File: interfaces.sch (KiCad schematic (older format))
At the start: 16 parts, among them U10 TDA19988BHN_C1,557

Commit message: Update naming convention
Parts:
- C37, C39, C41, C43: footprint arv-som-footprints:0402-cap -> arvsom-footprints:0402-cap; symbol arv-som:C_2u2_0402 -> arvsom:C_2u2_0402
- C38, C40, C42, C44: footprint arv-som-footprints:0201-res -> arvsom-footprints:0201-res; symbol arv-som:C_100n_0201 -> arvsom:C_100n_0201
- D3: footprint arv-som-footprints:SOD-323F -> arvsom-footprints:SOD-323F; symbol arv-som:1N4148WS -> arvsom:1N4148WS
- FB1, FB7: footprint arv-som-footprints:0402-res -> arvsom-footprints:0402-res; symbol arv-som:BLM15PD121SN1D -> arvsom:BLM15PD121SN1D
- R25: footprint arv-som-footprints:0402-res -> arvsom-footprints:0402-res; symbol arv-som:R_10k_0402 -> arvsom:R_10k_0402
- R26, R27: footprint arv-som-footprints:0402-res -> arvsom-footprints:0402-res; symbol arv-som:R_1k_0402 -> arvsom:R_1k_0402
- R28: footprint arv-som-footprints:0402-res -> arvsom-footprints:0402-res; symbol arv-som:R_27k_0402 -> arvsom:R_27k_0402
- U10: footprint arv-som-footprints:QFN50P900X900X100-65N -> arvsom-footprints:QFN50P900X900X100-65N; symbol arv-som:TDA19988BHN_C1,557 -> arvsom:TDA19988BHN_C1,557
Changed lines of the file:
@@
 $EndDescr
 $Comp
-L arv-som:TDA19988BHN_C1,557 U10
+L arvsom:TDA19988BHN_C1,557 U10
 U 1 1 607A5735
 P 7075 5525
 F 0 "U10" H 7075 8192 50  0000 C CNN
 F 1 "TDA19988BHN_C1,557" H 7075 8101 50  0000 C CNN
-F 2 "arv-som-footprints:QFN50P900X900X100-65N" H 7075 5525 50  0001 L BNN
+F 2 "arvsom-footprints:QFN50P900X900X100-65N" H 7075 5525 50  0001 L BNN
 F 3 "" H 7075 5525 50  0001 L BNN
 F 4 "NXP Semiconductors" H 7075 5525 50  0001 L BNN "MANUFACTURER"
@@
 Connection ~ 5975 3725
 $Comp
-L arv-som:GND #PWR0137
+L arvsom:GND #PWR0137
 U 1 1 607C5297
 P 5975 8125
@@
 Connection ~ 8375 3425
 $Comp
-L arv-som:C_2u2_0402 C37
+L arvsom:C_2u2_0402 C37
 U 1 1 607E47D0
 P 9125 3000
 F 0 "C37" H 9240 3045 60  0000 L CNN
 F 1 "C_2u2_0402" H 9125 2850 60  0001 C CNN
-F 2 "arv-som-footprints:0402-cap" H 9325 3200 60  0001 L CNN
+F 2 "arvsom-footprints:0402-cap" H 9325 3200 60  0001 L CNN
 F 3 "" H 9125 3000 50  0001 C CNN
 F 4 "TDK" H 9325 3400 60  0001 L CNN "Manufacturer"
@@
 $EndComp
 $Comp
-L arv-som:C_2u2_0402 C39
+L arvsom:C_2u2_0402 C39
 U 1 1 607E4C5F
 P 9900 3000
 F 0 "C39" H 10015 3045 60  0000 L CNN
 F 1 "C_2u2_0402" H 9900 2850 60  0001 C CNN
-F 2 "arv-som-footprints:0402-cap" H 10100 3200 60  0001 L CNN
+F 2 "arvsom-footprints:0402-cap" H 10100 3200 60  0001 L CNN
 F 3 "" H 9900 3000 50  0001 C CNN
 F 4 "TDK" H 10100 3400 60  0001 L CNN "Manufacturer"
@@
 HDMI_1V8
 $Comp
-L arv-som:GND #PWR0138
+L arvsom:GND #PWR0138
 U 1 1 607E87FB
 P 9125 3150
@@
 HDMI_1V8
 $Comp
-L arv-som:GND #PWR0139
+L arvsom:GND #PWR0139
 U 1 1 607EFCC2
 P 9900 3150
@@
 $EndComp
 $Comp
-L arv-som:C_2u2_0402 C41
+L arvsom:C_2u2_0402 C41
 U 1 1 607F1ECB
 P 10625 3000
 F 0 "C41" H 10740 3045 60  0000 L CNN
 F 1 "C_2u2_0402" H 10625 2850 60  0001 C CNN
-F 2 "arv-som-footprints:0402-cap" H 10825 3200 60  0001 L CNN
+F 2 "arvsom-footprints:0402-cap" H 10825 3200 60  0001 L CNN
 F 3 "" H 10625 3000 50  0001 C CNN
 F 4 "TDK" H 10825 3400 60  0001 L CNN "Manufacturer"
@@
 HDMI_1V8
 $Comp
-L arv-som:GND #PWR0140
+L arvsom:GND #PWR0140
 U 1 1 607F1ED2
 P 10625 3150
@@
 $EndComp
 $Comp
-L arv-som:C_2u2_0402 C43
+L arvsom:C_2u2_0402 C43
 U 1 1 607F4B71
 P 11375 3000
 F 0 "C43" H 11490 3045 60  0000 L CNN
 F 1 "C_2u2_0402" H 11375 2850 60  0001 C CNN
-F 2 "arv-som-footprints:0402-cap" H 11575 3200 60  0001 L CNN
+F 2 "arvsom-footprints:0402-cap" H 11575 3200 60  0001 L CNN
 F 3 "" H 11375 3000 50  0001 C CNN
 F 4 "TDK" H 11575 3400 60  0001 L CNN "Manufacturer"
@@
 HDMI_1V8
 $Comp
-L arv-som:GND #PWR0141
+L arvsom:GND #PWR0141
 U 1 1 607F4B78
 P 11375 3150
@@
 $EndComp
 $Comp
-L arv-som:C_100n_0201 C38
+L arvsom:C_100n_0201 C38
 U 1 1 607F7307
 P 9500 3000
 F 0 "C38" H 9615 3045 60  0000 L CNN
 F 1 "C_100n_0201" H 9500 2850 60  0001 C CNN
-F 2 "arv-som-footprints:0201-res" H 9700 3200 60  0001 L CNN
+F 2 "arvsom-footprints:0201-res" H 9700 3200 60  0001 L CNN
 F 3 "" H 9500 3000 50  0001 C CNN
 F 4 "YAGEO" H 9700 3400 60  0001 L CNN "Manufacturer"
@@
 HDMI_1V8
 $Comp
-L arv-som:GND #PWR0142
+L arvsom:GND #PWR0142
 U 1 1 607F77A7
 P 9500 3150
@@
 $EndComp
 $Comp
-L arv-som:C_100n_0201 C40
+L arvsom:C_100n_0201 C40
 U 1 1 607F8E18
 P 10275 3000
 F 0 "C40" H 10390 3045 60  0000 L CNN
 F 1 "C_100n_0201" H 10275 2850 60  0001 C CNN
-F 2 "arv-som-footprints:0201-res" H 10475 3200 60  0001 L CNN
+F 2 "arvsom-footprints:0201-res" H 10475 3200 60  0001 L CNN
 F 3 "" H 10275 3000 50  0001 C CNN
 F 4 "YAGEO" H 10475 3400 60  0001 L CNN "Manufacturer"
@@
 HDMI_1V8
 $Comp
-L arv-som:GND #PWR0143
+L arvsom:GND #PWR0143
 U 1 1 607F8E1F
 P 10275 3150
@@
 $EndComp
 $Comp
-L arv-som:C_100n_0201 C42
+L arvsom:C_100n_0201 C42
 U 1 1 607FB340
 P 11000 3000
 F 0 "C42" H 11115 3045 60  0000 L CNN
 F 1 "C_100n_0201" H 11000 2850 60  0001 C CNN
-F 2 "arv-som-footprints:0201-res" H 11200 3200 60  0001 L CNN
+F 2 "arvsom-footprints:0201-res" H 11200 3200 60  0001 L CNN
 F 3 "" H 11000 3000 50  0001 C CNN
 F 4 "YAGEO" H 11200 3400 60  0001 L CNN "Manufacturer"
@@
 HDMI_1V8
 $Comp
-L arv-som:GND #PWR0144
+L arvsom:GND #PWR0144
 U 1 1 607FB347
 P 11000 3150
@@
 $EndComp
 $Comp
-L arv-som:C_100n_0201 C44
+L arvsom:C_100n_0201 C44
 U 1 1 607FD800
 P 11750 3000
 F 0 "C44" H 11865 3045 60  0000 L CNN
 F 1 "C_100n_0201" H 11750 2850 60  0001 C CNN
-F 2 "arv-som-footprints:0201-res" H 11950 3200 60  0001 L CNN
+F 2 "arvsom-footprints:0201-res" H 11950 3200 60  0001 L CNN
 F 3 "" H 11750 3000 50  0001 C CNN
 F 4 "YAGEO" H 11950 3400 60  0001 L CNN "Manufacturer"
@@
 HDMI_1V8
 $Comp
-L arv-som:GND #PWR0145
+L arvsom:GND #PWR0145
 U 1 1 607FD807
 P 11750 3150
@@
 TODO: 2u2 with 0201 package
 $Comp
-L arv-som:BLM15PD121SN1D FB1
+L arvsom:BLM15PD121SN1D FB1
 U 1 1 6086D39A
 P 11325 2175
 F 0 "FB1" H 11325 2462 60  0000 C CNN
 F 1 "BLM15PD121SN1D" H 11325 2356 60  0000 C CNN
-F 2 "arv-som-footprints:0402-res" H 11525 2375 60  0001 L CNN
+F 2 "arvsom-footprints:0402-res" H 11525 2375 60  0001 L CNN
 F 3 "" H 11525 2475 60  0001 L CNN
 F 4 "BLM15PD121SN1D" H 11525 2675 60  0001 L CNN "MPN"
@@
 	8550 3725 8650 3725
 $Comp
-L arv-som:R_10k_0402 R25
+L arvsom:R_10k_0402 R25
 U 1 1 608924F4
 P 8800 3725
 F 0 "R25" H 8800 3938 60  0000 C CNN
 F 1 "R_10k_0402" H 8800 3575 60  0001 C CNN
-F 2 "arv-som-footprints:0402-res" H 9000 3925 60  0001 L CNN
+F 2 "arvsom-footprints:0402-res" H 9000 3925 60  0001 L CNN
 F 3 "" H 8800 3725 50  0001 C CNN
 F 4 "VISHAY" H 9000 4125 60  0001 L CNN "Manufacturer"
@@
 $EndComp
 $Comp
-L arv-som:GND #PWR0146
+L arvsom:GND #PWR0146
 U 1 1 60893600
 P 9050 3725
@@
 HDMI_DSDA
 $Comp
-L arv-som:R_1k_0402 R26
+L arvsom:R_1k_0402 R26
 U 1 1 608F44D4
 P 9025 6125
 F 0 "R26" H 8950 6225 60  0000 L CNN
 F 1 "R_1k_0402" H 9025 5975 60  0001 C CNN
-F 2 "arv-som-footprints:0402-res" H 9225 6325 60  0001 L CNN
+F 2 "arvsom-footprints:0402-res" H 9225 6325 60  0001 L CNN
 F 3 "" H 9025 6125 50  0001 C CNN
 F 4 "BOURNS" H 9225 6525 60  0001 L CNN "Manufacturer"
@@
 $EndComp
 $Comp
-L arv-som:R_1k_0402 R27
+L arvsom:R_1k_0402 R27
 U 1 1 608F47DE
 P 9275 6125
 F 0 "R27" H 9200 6225 60  0000 L CNN
 F 1 "R_1k_0402" H 9275 5975 60  0001 C CNN
-F 2 "arv-som-footprints:0402-res" H 9475 6325 60  0001 L CNN
+F 2 "arvsom-footprints:0402-res" H 9475 6325 60  0001 L CNN
 F 3 "" H 9275 6125 50  0001 C CNN
 F 4 "BOURNS" H 9475 6525 60  0001 L CNN "Manufacturer"
@@
 HDMI_HPD
 $Comp
-L arv-som:1N4148WS D3
+L arvsom:1N4148WS D3
 U 1 1 60934FA2
 P 9225 6950
 F 0 "D3" H 9025 6900 60  0000 C CNN
 F 1 "1N4148WS" H 9575 6900 60  0000 C CNN
-F 2 "arv-som-footprints:SOD-323F" H 9425 7150 60  0001 L CNN
+F 2 "arvsom-footprints:SOD-323F" H 9425 7150 60  0001 L CNN
 F 3 "https://www.onsemi.com/pub/Collateral/1N914BWS-D.pdf" H 9425 7250 60  0001 L CNN
 F 4 "1N4148WS" H 9425 7450 60  0001 L CNN "MPN"
@@
 	8950 7125 9425 7125
 $Comp
-L arv-som:R_27k_0402 R28
+L arvsom:R_27k_0402 R28
 U 1 1 6093E329
 P 9700 6950
 F 0 "R28" H 9700 7050 60  0000 C CNN
 F 1 "R_27k_0402" H 9700 6800 60  0001 C CNN
-F 2 "arv-som-footprints:0402-res" H 9900 7150 60  0001 L CNN
+F 2 "arvsom-footprints:0402-res" H 9900 7150 60  0001 L CNN
 F 3 "" H 9700 6950 50  0001 C CNN
 F 4 "PANASONIC_ELECTRONIC_COMPONENTS" H 9900 7350 60  0001 L CNN "Manufacturer"
@@
 	8225 7825 8225 7925
 $Comp
-L arv-som:GND #PWR0147
+L arvsom:GND #PWR0147
 U 1 1 6095A132
 P 8225 8125
@@
 $EndBitmap
 $Comp
-L arv-som:BLM15PD121SN1D FB7
+L arvsom:BLM15PD121SN1D FB7
 U 1 1 60D6E8D3
 P 9025 5700
 F 0 "FB7" H 9025 5987 60  0000 C CNN
 F 1 "BLM15PD121SN1D" H 9025 5881 60  0000 C CNN
-F 2 "arv-som-footprints:0402-res" H 9225 5900 60  0001 L CNN
+F 2 "arvsom-footprints:0402-res" H 9225 5900 60  0001 L CNN
 F 3 "" H 9225 6000 60  0001 L CNN
 F 4 "BLM15PD121SN1D" H 9225 6200 60  0001 L CNN "MPN"

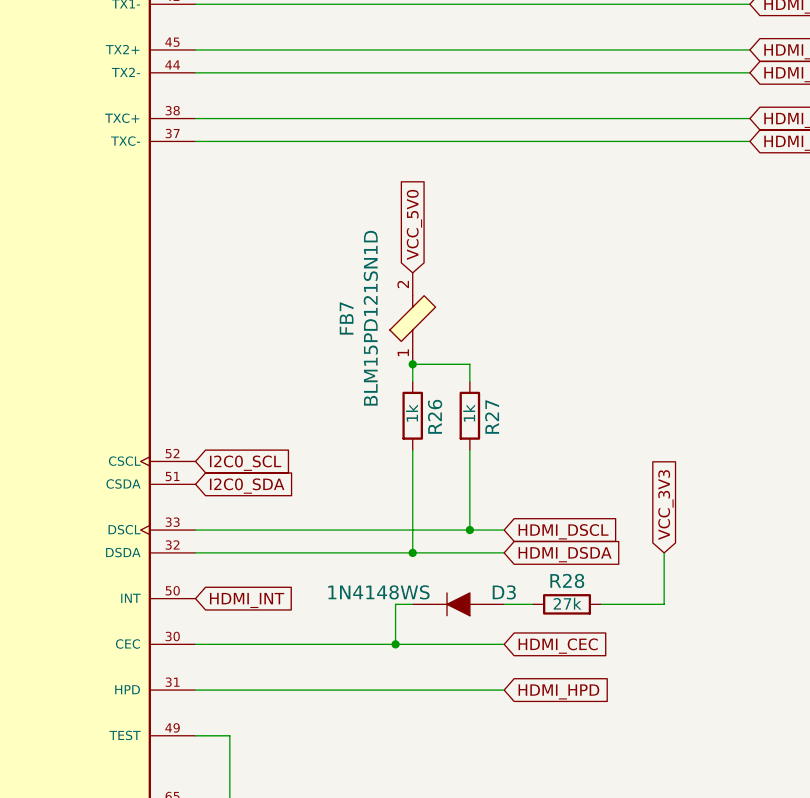
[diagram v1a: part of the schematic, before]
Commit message: Updated ethernet and interfaces.sch
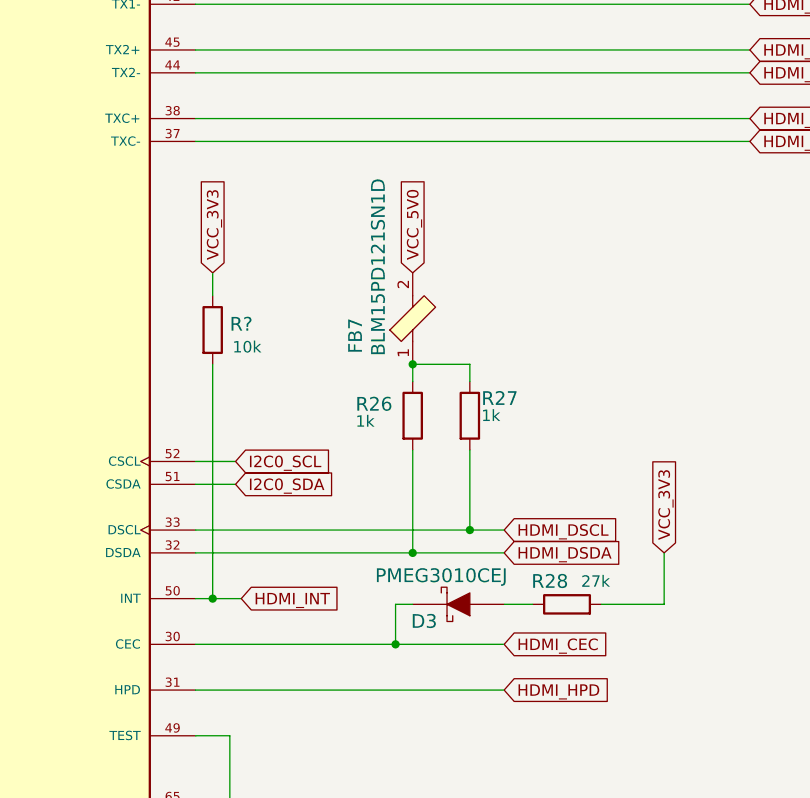
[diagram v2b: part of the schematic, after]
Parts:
- removed D3: 1N4148WS, arvsom-footprints:SOD-323F, symbol arvsom:1N4148WS
- added D3: PMEG3010CEJ, arvsom-footprints:SOD-323F, symbol arvsom:PMEG3010CEJ
- added R?: R_10k_0402, arvsom-footprints:0402-res, symbol arvsom:R_10k_0402
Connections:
- net HDMI_CEC: now also D3.K
- net HDMI_INT: now also R?.2
- net VCC_3V3: now also R?.1
- net at R28.1: now also D3.A
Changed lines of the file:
@@
 U 1 1 608F44D4
 P 9025 6125
-F 0 "R26" H 8950 6225 60  0000 L CNN
+F 0 "R26" V 8975 5875 60  0000 L CNN
 F 1 "R_1k_0402" H 9025 5975 60  0001 C CNN
 F 2 "arvsom-footprints:0402-res" H 9225 6325 60  0001 L CNN
@@
 F 4 "BOURNS" H 9225 6525 60  0001 L CNN "Manufacturer"
 F 5 "CR0402-FX-1001GLF" H 9225 6425 60  0001 L CNN "MPN"
-F 6 "1k" H 8975 6125 50  0000 L CNN "Val"
+F 6 "1k" V 9050 5875 50  0000 L CNN "Val"
 	1    9025 6125
 	0    1    1    0
@@
 U 1 1 608F47DE
 P 9275 6125
-F 0 "R27" H 9200 6225 60  0000 L CNN
+F 0 "R27" V 9200 6175 60  0000 L CNN
 F 1 "R_1k_0402" H 9275 5975 60  0001 C CNN
 F 2 "arvsom-footprints:0402-res" H 9475 6325 60  0001 L CNN
@@
 F 4 "BOURNS" H 9475 6525 60  0001 L CNN "Manufacturer"
 F 5 "CR0402-FX-1001GLF" H 9475 6425 60  0001 L CNN "MPN"
-F 6 "1k" H 9225 6125 50  0000 L CNN "Val"
+F 6 "1k" V 9275 6175 50  0000 L CNN "Val"
 	1    9275 6125
 	0    1    1    0
 $EndComp
-Text GLabel 8075 6325 2    50   Input ~ 0
+Text GLabel 8250 6325 2    50   Input ~ 0
 I2C0_SCL
-Text GLabel 8075 6425 2    50   Input ~ 0
+Text GLabel 8250 6425 2    50   Input ~ 0
 I2C0_SDA
 Wire Wire Line
@@
 Text GLabel 9425 7325 2    50   Input ~ 0
 HDMI_HPD
-$Comp
-L arvsom:1N4148WS D3
-U 1 1 60934FA2
-P 9225 6950
-F 0 "D3" H 9025 6900 60  0000 C CNN
-F 1 "1N4148WS" H 9575 6900 60  0000 C CNN
-F 2 "arvsom-footprints:SOD-323F" H 9425 7150 60  0001 L CNN
-F 3 "https://www.onsemi.com/pub/Collateral/1N914BWS-D.pdf" H 9425 7250 60  0001 L CNN
-F 4 "1N4148WS" H 9425 7450 60  0001 L CNN "MPN"
-F 5 "ON Semiconductor" H 9425 8050 60  0001 L CNN "Manufacturer"
-	1    9225 6950
-	-1   0    0    1
-$EndComp
 Wire Wire Line
 	8075 7125 8950 7125
@@
 U 1 1 6093E329
 P 9700 6950
-F 0 "R28" H 9700 7050 60  0000 C CNN
+F 0 "R28" H 9625 7050 60  0000 C CNN
 F 1 "R_27k_0402" H 9700 6800 60  0001 C CNN
 F 2 "arvsom-footprints:0402-res" H 9900 7150 60  0001 L CNN
@@
 F 4 "PANASONIC_ELECTRONIC_COMPONENTS" H 9900 7350 60  0001 L CNN "Manufacturer"
 F 5 "ERJ2RKF2702X" H 9900 7250 60  0001 L CNN "MPN"
-F 6 "27k" H 9700 6950 50  0000 C CNN "Val"
+F 6 "27k" H 9825 7050 50  0000 C CNN "Val"
 	1    9700 6950
 	1    0    0    -1
@@
 Text GLabel 10125 6725 1    50   Input ~ 0
 VCC_3V3
-Text GLabel 8075 6925 2    50   Input ~ 0
+Text GLabel 8275 6925 2    50   Input ~ 0
 HDMI_INT
 Wire Wire Line
@@
 U 1 1 60D6E8D3
 P 9025 5700
-F 0 "FB7" H 9025 5987 60  0000 C CNN
-F 1 "BLM15PD121SN1D" H 9025 5881 60  0000 C CNN
+F 0 "FB7" H 8950 5950 60  0000 C CNN
+F 1 "BLM15PD121SN1D" H 9250 5850 60  0000 C CNN
 F 2 "arvsom-footprints:0402-res" H 9225 5900 60  0001 L CNN
 F 3 "" H 9225 6000 60  0001 L CNN
@@
 $EndComp
 Connection ~ 9025 5900
+$Comp
+L arvsom:PMEG3010CEJ D?
+U 1 1 60946B44
+P 9225 6950
+AR Path="/60751C8D/60946B44" Ref="D?"  Part="1"
+AR Path="/607858CA/60946B44" Ref="D3"  Part="1"
+F 0 "D3" H 9375 7025 60  0000 C CNN
+F 1 "PMEG3010CEJ" H 9300 6825 60  0000 C CNN
+F 2 "arvsom-footprints:SOD-323F" H 9425 7150 60  0001 L CNN
+F 3 "https://assets.nexperia.com/documents/data-sheet/PMEG3010CEH_PMEG3010CEJ.pdf" H 9425 7250 60  0001 L CNN
+F 4 "PMEG3010CEJ" H 9425 7450 60  0001 L CNN "MPN"
+F 5 "Nexperia" H 9425 8050 60  0001 L CNN "Manufacturer"
+	1    9225 6950
+	-1   0    0    1
+$EndComp
+Wire Wire Line
+	8250 6325 8075 6325
+Wire Wire Line
+	8075 6425 8250 6425
+Wire Wire Line
+	8275 6925 8150 6925
+$Comp
+L arvsom:R_10k_0402 R?
+U 1 1 6095B9AC
+P 8150 5750
+F 0 "R?" V 8125 5875 60  0000 C CNN
+F 1 "R_10k_0402" H 8150 5600 60  0001 C CNN
+F 2 "arvsom-footprints:0402-res" H 8350 5950 60  0001 L CNN
+F 3 "" H 8150 5750 50  0001 C CNN
+F 4 "VISHAY" H 8350 6150 60  0001 L CNN "Manufacturer"
+F 5 "CRCW040210K0FKEDHP" H 8350 6050 60  0001 L CNN "MPN"
+F 6 "10k" V 8225 5900 50  0000 C CNN "Val"
+	1    8150 5750
+	0    1    1    0
+$EndComp
+Text GLabel 8150 5500 1    50   Input ~ 0
+VCC_3V3
+Wire Wire Line
+	8150 5500 8150 5600
+Wire Wire Line
+	8150 5900 8150 6925
+Connection ~ 8150 6925
+Wire Wire Line
+	8150 6925 8075 6925
 $EndSCHEMATC

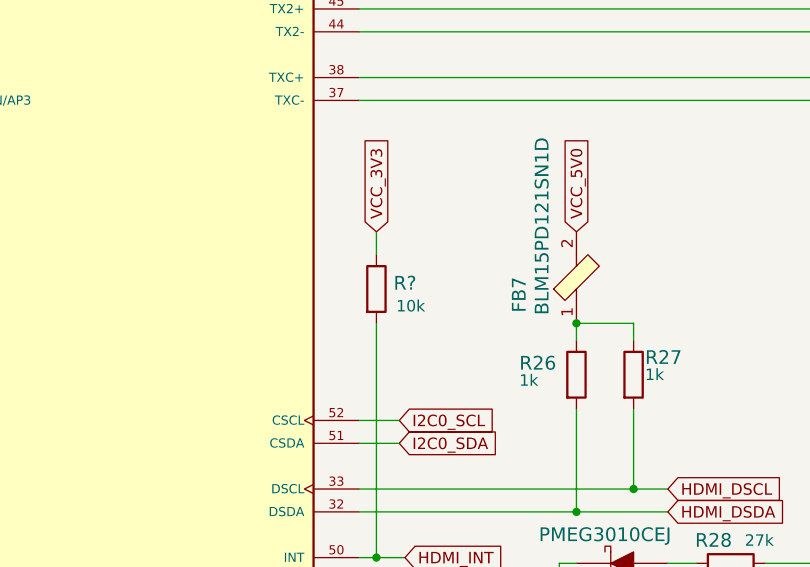
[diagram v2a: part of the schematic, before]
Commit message: Updated VIC config, added reset and crystals
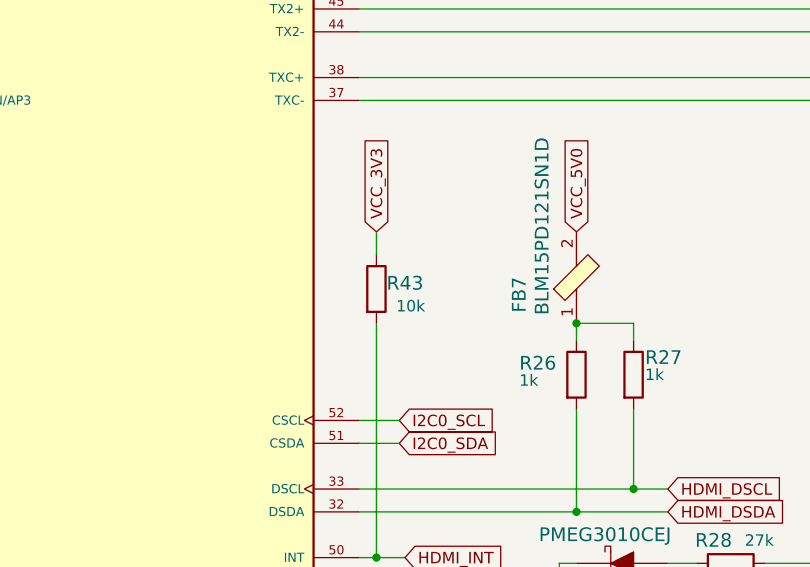
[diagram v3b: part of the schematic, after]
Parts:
- gave numbers to parts that had none: 1
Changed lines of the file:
@@
 	8275 6925 8150 6925
 $Comp
-L arvsom:R_10k_0402 R?
+L arvsom:R_10k_0402 R43
 U 1 1 6095B9AC
 P 8150 5750
-F 0 "R?" V 8125 5875 60  0000 C CNN
+F 0 "R43" V 8125 5875 60  0000 C CNN
 F 1 "R_10k_0402" H 8150 5600 60  0001 C CNN
 F 2 "arvsom-footprints:0402-res" H 8350 5950 60  0001 L CNN
